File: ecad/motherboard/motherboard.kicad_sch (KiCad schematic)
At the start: 16 parts, among them J1 B6B-XH-A(LF)(SN), U1 CD4051BPWR4, U2 NodeMCU ESP-32S

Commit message: Add manufacturer part numbers into Kicad Schematics
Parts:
- C1, C2: MPN (none) -> C0603C104M5RACTU; Manufacturer (none) -> KEMET
- J1: MPN (none) -> B6B-XH-A(LF)(SN); Manufacturer (none) -> JST
- R1, R2, R3: MPN (none) -> RC0603JR-1010KL; Manufacturer (none) -> Yageo; notes (none) -> pull up
- TP1, TP2, TP4, TP5, TP6, TP7, TP8: now left out of the parts list
- U1: MPN (none) -> CD4051BPWR; Manufacturer (none) -> TI
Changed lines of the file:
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@@
+      (effects (font (size 1.27 1.27)) hide)
+    )
+    (property "notes" "pull up" (at 185.42 123.19 0)
+      (effects (font (size 1.27 1.27)) hide)
+    )
+    (property "MPN" "RC0603JR-1010KL" (at 185.42 123.19 0)
+      (effects (font (size 1.27 1.27)) hide)
+    )
+    (property "Manufacturer" "Yageo" (at 185.42 123.19 0)
       (effects (font (size 1.27 1.27)) hide)
     )
@@
     )
     (property "Datasheet" "" (at 116.84 105.41 90)
+      (effects (font (size 1.27 1.27)) hide)
+    )
+    (property "notes" "" (at 123.19 97.79 0)
+      (effects (font (size 1.27 1.27)) hide)
+    )
+    (property "MPN" "B6B-XH-A(LF)(SN)" (at 123.19 97.79 0)
+      (effects (font (size 1.27 1.27)) hide)
+    )
+    (property "Manufacturer" "JST" (at 123.19 97.79 0)
       (effects (font (size 1.27 1.27)) hide)
     )
@@
     )
     (property "Datasheet" "https://www.ti.com/lit/ds/symlink/cd4051b.pdf" (at 82.55 123.19 0)
+      (effects (font (size 1.27 1.27)) hide)
+    )
+    (property "notes" "" (at 68.58 110.49 0)
+      (effects (font (size 1.27 1.27)) hide)
+    )
+    (property "MPN" "CD4051BPWR" (at 68.58 110.49 0)
+      (effects (font (size 1.27 1.27)) hide)
+    )
+    (property "Manufacturer" "TI" (at 68.58 110.49 0)
       (effects (font (size 1.27 1.27)) hide)
     )
@@
       (effects (font (size 1.27 1.27)) hide)
     )
+    (property "notes" "pull up" (at 179.07 123.19 0)
+      (effects (font (size 1.27 1.27)) hide)
+    )
+    (property "MPN" "RC0603JR-1010KL" (at 179.07 123.19 0)
+      (effects (font (size 1.27 1.27)) hide)
+    )
+    (property "Manufacturer" "Yageo" (at 179.07 123.19 0)
+      (effects (font (size 1.27 1.27)) hide)
+    )
     (pin "1")
     (pin "2")
@@
       (effects (font (size 1.27 1.27)) hide)
     )
+    (property "notes" "" (at 132.08 123.19 0)
+      (effects (font (size 1.27 1.27)) hide)
+    )
+    (property "MPN" "" (at 132.08 123.19 0)
+      (effects (font (size 1.27 1.27)) hide)
+    )
+    (property "Manufacturer" "" (at 132.08 123.19 0)
+      (effects (font (size 1.27 1.27)) hide)
+    )
     (pin "1")
     (instances
@@
   )
   (symbol (lib_id "Connector:TestPoint") (at 57.15 125.73 90) (unit 1)
-    (in_bom yes) (on_board yes) (dnp no)
+    (in_bom no) (on_board yes) (dnp no)
     (property "Reference" "TP2" (at 50.8 125.73 90)
       (effects (font (size 1.27 1.27)))
@@
       (effects (font (size 1.27 1.27)) hide)
     )
+    (property "notes" "" (at 57.15 125.73 0)
+      (effects (font (size 1.27 1.27)) hide)
+    )
+    (property "MPN" "" (at 57.15 125.73 0)
+      (effects (font (size 1.27 1.27)) hide)
+    )
+    (property "Manufacturer" "" (at 57.15 125.73 0)
+      (effects (font (size 1.27 1.27)) hide)
+    )
     (pin "1")
     (instances
@@
   )
   (symbol (lib_id "Connector:TestPoint") (at 132.08 153.67 90) (unit 1)
-    (in_bom yes) (on_board yes) (dnp no)
+    (in_bom no) (on_board yes) (dnp no)
     (property "Reference" "TP8" (at 125.73 153.67 90)
       (effects (font (size 1.27 1.27)))
@@
       (effects (font (size 1.27 1.27)) hide)
     )
+    (property "notes" "" (at 132.08 153.67 0)
+      (effects (font (size 1.27 1.27)) hide)
+    )
+    (property "MPN" "" (at 132.08 153.67 0)
+      (effects (font (size 1.27 1.27)) hide)
+    )
+    (property "Manufacturer" "" (at 132.08 153.67 0)
+      (effects (font (size 1.27 1.27)) hide)
+    )
     (pin "1")
     (instances
@@
   )
   (symbol (lib_id "Connector:TestPoint") (at 132.08 148.59 90) (unit 1)
-    (in_bom yes) (on_board yes) (dnp no)
+    (in_bom no) (on_board yes) (dnp no)
     (property "Reference" "TP6" (at 125.73 148.59 90)
       (effects (font (size 1.27 1.27)))
@@
       (effects (font (size 1.27 1.27)) hide)
     )
+    (property "notes" "" (at 132.08 148.59 0)
+      (effects (font (size 1.27 1.27)) hide)
+    )
+    (property "MPN" "" (at 132.08 148.59 0)
+      (effects (font (size 1.27 1.27)) hide)
+    )
+    (property "Manufacturer" "" (at 132.08 148.59 0)
+      (effects (font (size 1.27 1.27)) hide)
+    )
     (pin "1")
     (instances
@@
   )
   (symbol (lib_id "Connector:TestPoint") (at 132.08 151.13 90) (unit 1)
-    (in_bom yes) (on_board yes) (dnp no)
+    (in_bom no) (on_board yes) (dnp no)
     (property "Reference" "TP7" (at 125.73 151.13 90)
       (effects (font (size 1.27 1.27)))
@@
     )
     (property "Datasheet" "~" (at 132.08 146.05 0)
+      (effects (font (size 1.27 1.27)) hide)
+    )
+    (property "notes" "" (at 132.08 151.13 0)
+      (effects (font (size 1.27 1.27)) hide)
+    )
+    (property "MPN" "" (at 132.08 151.13 0)
+      (effects (font (size 1.27 1.27)) hide)
+    )
+    (property "Manufacturer" "" (at 132.08 151.13 0)
       (effects (font (size 1.27 1.27)) hide)
     )
@@
       (effects (font (size 1.27 1.27)) hide)
     )
+    (property "notes" "" (at 100.33 116.84 0)
+      (effects (font (size 1.27 1.27)) hide)
+    )
+    (property "MPN" "C0603C104M5RACTU" (at 100.33 116.84 0)
+      (effects (font (size 1.27 1.27)) hide)
+    )
+    (property "Manufacturer" "KEMET " (at 100.33 116.84 0)
+      (effects (font (size 1.27 1.27)) hide)
+    )
     (pin "1")
     (pin "2")
@@
   )
   (symbol (lib_id "Connector:TestPoint") (at 132.08 128.27 90) (unit 1)
-    (in_bom yes) (on_board yes) (dnp no)
+    (in_bom no) (on_board yes) (dnp no)
     (property "Reference" "TP4" (at 125.73 128.27 90)
       (effects (font (size 1.27 1.27)))
@@
     )
     (property "Datasheet" "~" (at 132.08 123.19 0)
+      (effects (font (size 1.27 1.27)) hide)
+    )
+    (property "notes" "" (at 132.08 128.27 0)
+      (effects (font (size 1.27 1.27)) hide)
+    )
+    (property "MPN" "" (at 132.08 128.27 0)
+      (effects (font (size 1.27 1.27)) hide)
+    )
+    (property "Manufacturer" "" (at 132.08 128.27 0)
       (effects (font (size 1.27 1.27)) hide)
     )
@@
       (effects (font (size 1.27 1.27)) hide)
     )
+    (property "notes" "pull up" (at 191.77 123.19 0)
+      (effects (font (size 1.27 1.27)) hide)
+    )
+    (property "MPN" "RC0603JR-1010KL" (at 191.77 123.19 0)
+      (effects (font (size 1.27 1.27)) hide)
+    )
+    (property "Manufacturer" "Yageo" (at 191.77 123.19 0)
+      (effects (font (size 1.27 1.27)) hide)
+    )
     (pin "1")
     (pin "2")
@@
     )
     (property "Datasheet" "" (at 134.62 116.84 0)
+      (effects (font (size 1.27 1.27)) hide)
+    )
+    (property "notes" "" (at 148.59 142.24 0)
+      (effects (font (size 1.27 1.27)) hide)
+    )
+    (property "MPN" "" (at 148.59 142.24 0)
+      (effects (font (size 1.27 1.27)) hide)
+    )
+    (property "Manufacturer" "" (at 148.59 142.24 0)
       (effects (font (size 1.27 1.27)) hide)
     )
@@
   )
   (symbol (lib_id "Connector:TestPoint") (at 132.08 146.05 90) (unit 1)
-    (in_bom yes) (on_board yes) (dnp no)
+    (in_bom no) (on_board yes) (dnp no)
     (property "Reference" "TP5" (at 125.73 146.05 90)
       (effects (font (size 1.27 1.27)))
@@
     )
     (property "Datasheet" "~" (at 132.08 140.97 0)
+      (effects (font (size 1.27 1.27)) hide)
+    )
+    (property "notes" "" (at 132.08 146.05 0)
+      (effects (font (size 1.27 1.27)) hide)
+    )
+    (property "MPN" "" (at 132.08 146.05 0)
+      (effects (font (size 1.27 1.27)) hide)
+    )
+    (property "Manufacturer" "" (at 132.08 146.05 0)
       (effects (font (size 1.27 1.27)) hide)
     )
@@
       (effects (font (size 1.27 1.27)) hide)
     )
+    (property "notes" "" (at 171.45 119.38 0)
+      (effects (font (size 1.27 1.27)) hide)
+    )
+    (property "MPN" "C0603C104M5RACTU" (at 171.45 119.38 0)
+      (effects (font (size 1.27 1.27)) hide)
+    )
+    (property "Manufacturer" "KEMET " (at 171.45 119.38 0)
+      (effects (font (size 1.27 1.27)) hide)
+    )
     (pin "1")
     (pin "2")
@@
   )
   (symbol (lib_id "Connector:TestPoint") (at 57.15 123.19 90) (unit 1)
-    (in_bom yes) (on_board yes) (dnp no)
+    (in_bom no) (on_board yes) (dnp no)
     (property "Reference" "TP1" (at 50.8 123.19 90)
       (effects (font (size 1.27 1.27)))
@@
       (effects (font (size 1.27 1.27)) hide)
     )
+    (property "notes" "" (at 57.15 123.19 0)
+      (effects (font (size 1.27 1.27)) hide)
+    )
+    (property "MPN" "" (at 57.15 123.19 0)
+      (effects (font (size 1.27 1.27)) hide)
+    )
+    (property "Manufacturer" "" (at 57.15 123.19 0)
+      (effects (font (size 1.27 1.27)) hide)
+    )

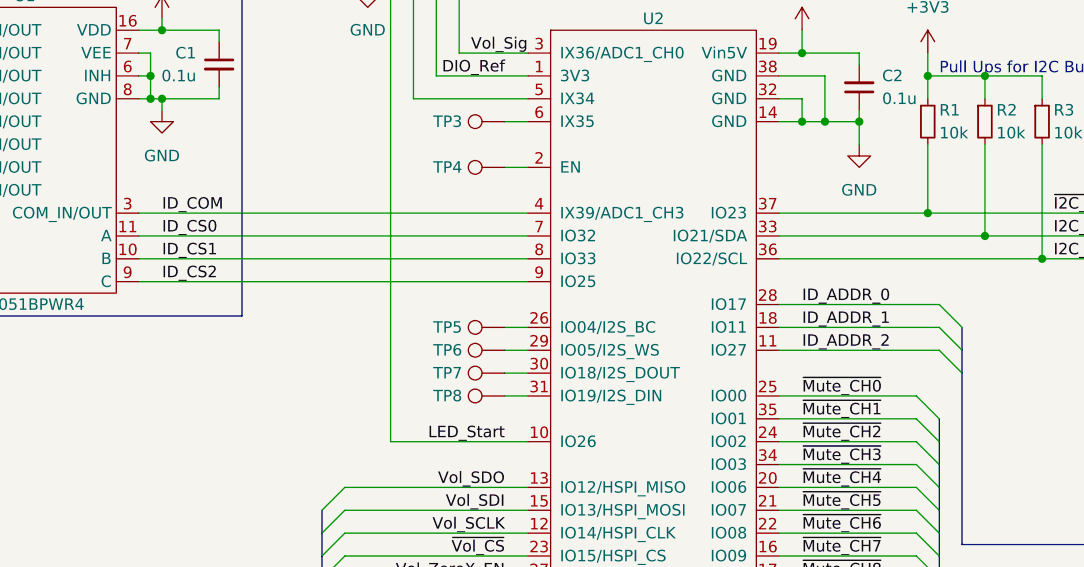
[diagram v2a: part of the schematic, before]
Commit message: Update Net labels for better consistency.
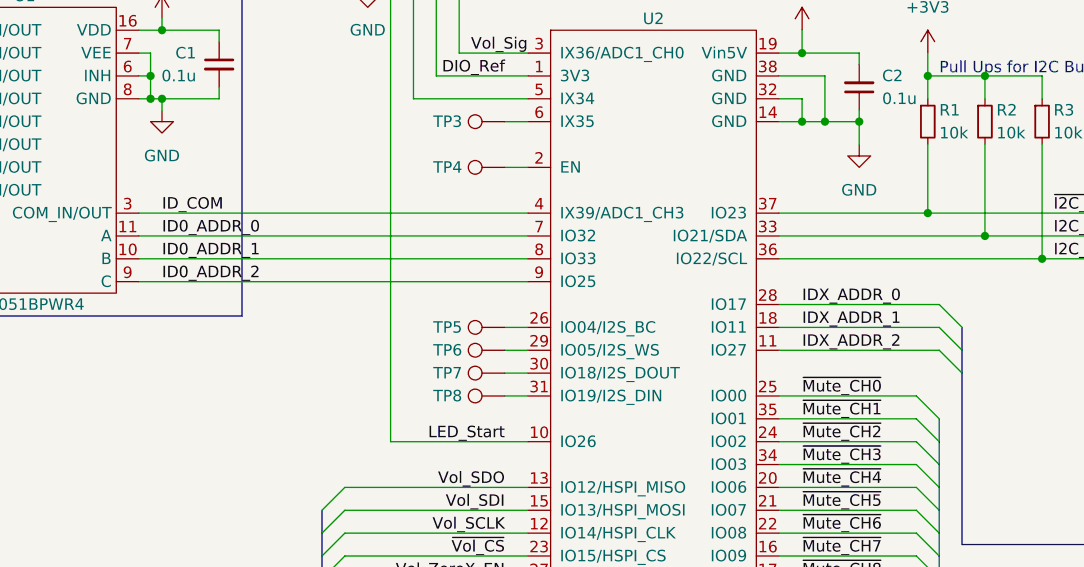
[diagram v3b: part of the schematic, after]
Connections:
- net ID_ADDR_0: no longer U2.28 (IO17)
- net ID_ADDR_1: no longer U2.18 (IO11)
- net ID_ADDR_2: no longer U2.11 (IO27)
- net ID_CS0 renamed ID0_ADDR_0
- net ID_CS1 renamed ID0_ADDR_1
- net ID_CS2 renamed ID0_ADDR_2
- new net IDX_ADDR_0: U2.28 (IO17)
- new net IDX_ADDR_1: U2.18 (IO11)
- new net IDX_ADDR_2: U2.11 (IO27)
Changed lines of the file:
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@@
     (effects (font (size 1.27 1.27)) (justify right bottom))
-  )
-  (label "ID_CS0" (at 93.98 135.89 0) (fields_autoplaced)
-    (effects (font (size 1.27 1.27)) (justify left bottom))
   )
   (label "{~{I2C_INT} I2C_SDA I2C_SCL}" (at 204.47 142.24 0) (fields_autoplaced)
@@
     (effects (font (size 1.27 1.27)) (justify left bottom))
   )
-  (label "ID_ADDR_1" (at 165.1 146.05 0) (fields_autoplaced)
+  (label "IDX_ADDR_1" (at 165.1 146.05 0) (fields_autoplaced)
     (effects (font (size 1.27 1.27)) (justify left bottom))
   )
@@
     (effects (font (size 1.27 1.27)) (justify right bottom))
   )
-  (label "ID_ADDR_2" (at 165.1 148.59 0) (fields_autoplaced)
+  (label "IDX_ADDR_2" (at 165.1 148.59 0) (fields_autoplaced)
     (effects (font (size 1.27 1.27)) (justify left bottom))
   )
@@
     (effects (font (size 1.27 1.27)) (justify right bottom))
   )
-  (label "ID_ADDR_0" (at 165.1 143.51 0) (fields_autoplaced)
+  (label "IDX_ADDR_0" (at 165.1 143.51 0) (fields_autoplaced)
     (effects (font (size 1.27 1.27)) (justify left bottom))
   )
@@
     (effects (font (size 1.27 1.27)) (justify right bottom))
   )
-  (label "ID_CS2" (at 93.98 140.97 0) (fields_autoplaced)
-    (effects (font (size 1.27 1.27)) (justify left bottom))
-  )
   (label "Vol_SDI" (at 342.9 127 180) (fields_autoplaced)
     (effects (font (size 1.27 1.27)) (justify right bottom))
-  )
-  (label "ID_CS1" (at 93.98 138.43 0) (fields_autoplaced)
-    (effects (font (size 1.27 1.27)) (justify left bottom))
   )
   (label "I2C_SCL" (at 260.35 127 180) (fields_autoplaced)
@@
     (effects (font (size 1.27 1.27)) (justify left bottom))
   )
+  (label "ID0_ADDR_2" (at 93.98 140.97 0) (fields_autoplaced)
+    (effects (font (size 1.27 1.27)) (justify left bottom))
+  )
   (label "I2C_SDA" (at 260.35 124.46 180) (fields_autoplaced)
     (effects (font (size 1.27 1.27)) (justify right bottom))
@@
     (effects (font (size 1.27 1.27)) (justify left bottom))
   )
+  (label "ID0_ADDR_0" (at 93.98 135.89 0) (fields_autoplaced)
+    (effects (font (size 1.27 1.27)) (justify left bottom))
+  )
   (label "ID_COM_0" (at 63.5 113.03 180) (fields_autoplaced)
     (effects (font (size 1.27 1.27)) (justify right bottom))
   )
+  (label "ID0_ADDR_1" (at 93.98 138.43 0) (fields_autoplaced)
+    (effects (font (size 1.27 1.27)) (justify left bottom))
+  )
   (label "I2C_SCL" (at 193.04 138.43 0) (fields_autoplaced)
